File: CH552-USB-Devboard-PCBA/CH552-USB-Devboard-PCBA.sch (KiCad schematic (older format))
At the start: 42 parts, among them J1 Conn_01x11_Male, J2 Conn_01x11_Male, J3 USB_C_Receptacle, J4 USB_C_Receptacle, SW1 SW_Push, SW2 SW_Push, U2 CH552G, U3 TPS7A4101DGNT

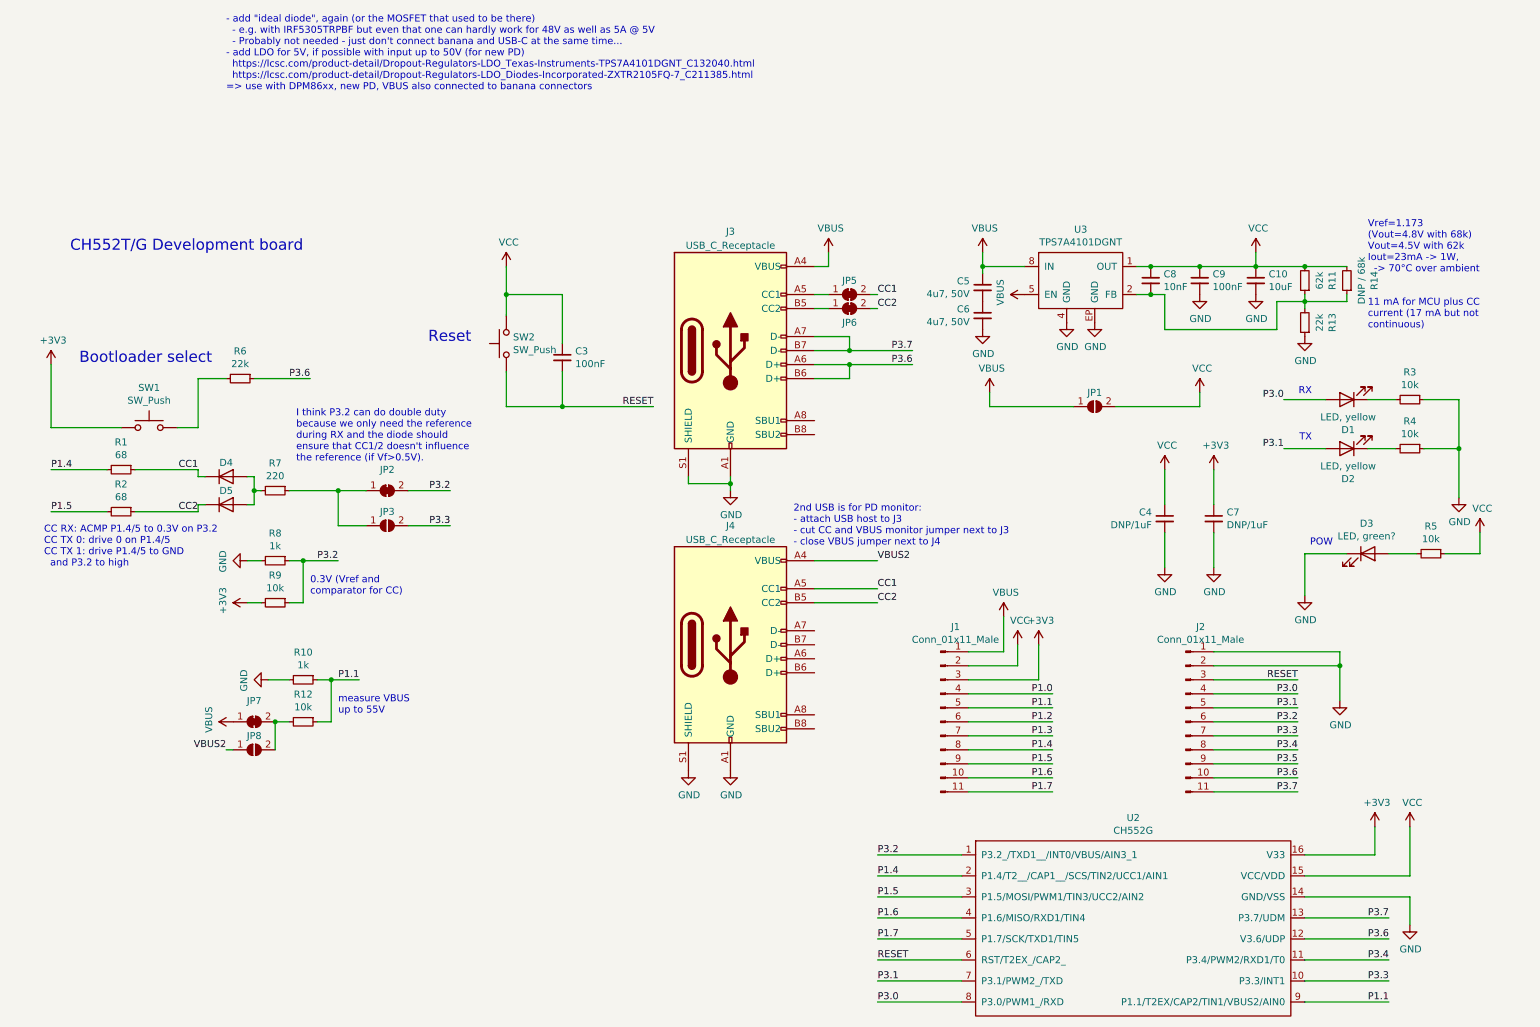
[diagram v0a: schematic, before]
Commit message: create variant for PCBA
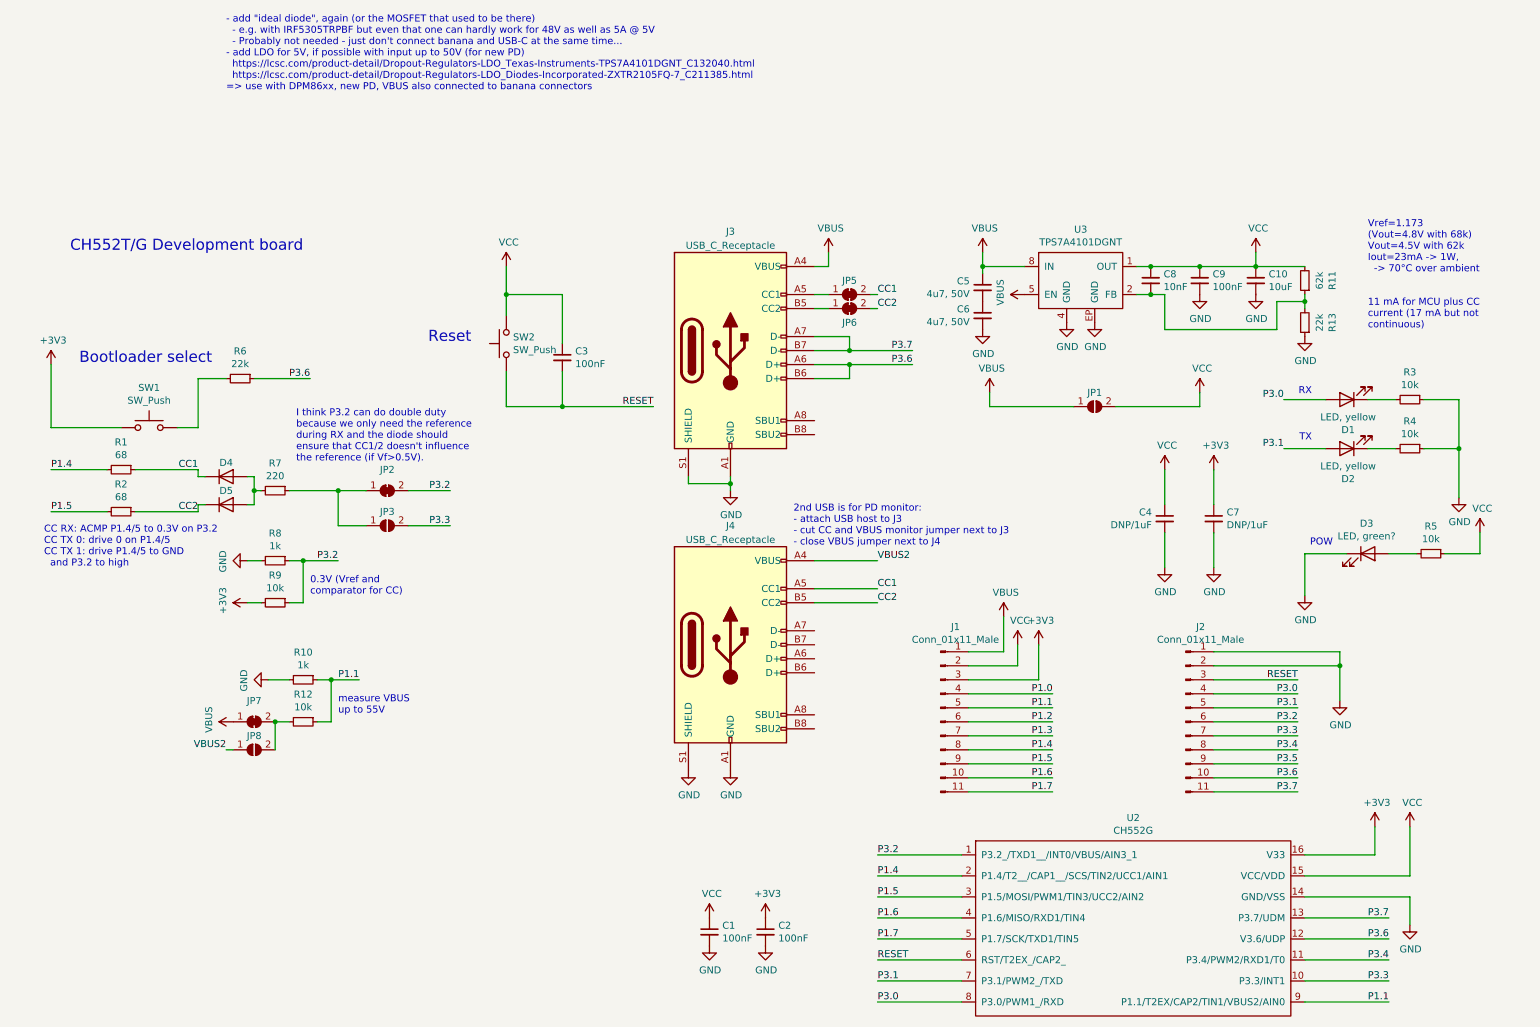
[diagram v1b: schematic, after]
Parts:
- removed R14: DNP / 68k, Resistor_SMD:R_0603_1608Metric_Pad1.05x0.95mm_HandSolder, symbol Device:R_Small
- added C1, C2: 100nF, Capacitor_SMD:C_0603_1608Metric_Pad1.05x0.95mm_HandSolder, symbol Device:C_Small
- J4: footprint footprint:VACON_CSP_USC16_TR -> CH552-USB-Devboard:Korean-Hroparts-Elec-TYPE-C-31-M-17; LCSC C165948 -> C283540
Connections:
- net +3V3: now also C2.1
- net GND: now also C1.2, C2.2
- net VCC: now also C1.1
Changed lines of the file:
@@
 EESchema Schematic File Version 4
+LIBS:CH552-USB-Devboard-PCBA-cache
 EELAYER 29 0
 EELAYER END
@@
 F 0 "J4" H 5650 4400 50  0000 C CNN
 F 1 "USB_C_Receptacle" H 5650 4300 50  0000 C CNN
-F 2 "footprint:VACON_CSP_USC16_TR" H 5800 3550 50  0001 C CNN
+F 2 "CH552-USB-Devboard:Korean-Hroparts-Elec-TYPE-C-31-M-17" H 5800 3550 50  0001 C CNN
 F 3 "http://www.usb.org/developers/docs/usb_31_033017.zip" H 5800 3550 50  0001 C CNN
-F 4 "C165948" H 5650 3550 50  0001 C CNN "LCSC"
+F 4 "C283540" H 5650 3550 50  0001 C CNN "LCSC"
 F 5 "PCBA" H 5650 3550 50  0001 C CNN "DNP"
 	1    5650 3550
@@
 Text Notes 10200 900  0    50   ~ 0
 Vref=1.173\n(Vout=4.8V with 68k)\nVout=4.5V with 62k\nIout=23mA -> 1W,\n  -> 70°C over ambient
-$Comp
-L Device:R_Small R14
-U 1 1 60E7CBB2
-P 10050 950
-F 0 "R14" V 9854 950 50  0000 C CNN
-F 1 "DNP / 68k" V 9945 950 50  0000 C CNN
-F 2 "Resistor_SMD:R_0603_1608Metric_Pad1.05x0.95mm_HandSolder" H 10050 950 50  0001 C CNN
-F 3 "~" H 10050 950 50  0001 C CNN
-F 4 "C23231" V 10050 950 50  0001 C CNN "LCSC"
-F 5 "1" V 10050 950 50  0001 C CNN "DNP"
-	1    10050 950
-	-1   0    0    1
-$EndComp
-Wire Wire Line
-	9750 1100 10050 1100
-Wire Wire Line
-	10050 1100 10050 1050
-Wire Wire Line
-	10050 850  9750 850
-Connection ~ 9750 850
 Text Notes 10200 1300 0    50   ~ 0
 11 mA for MCU plus CC\ncurrent (17 mA but not\ncontinuous)
@@
 	1    0    0    -1
 $EndComp
+$Comp
+L Device:C_Small C2
+U 1 1 60D50D65
+P 5900 5600
+F 0 "C2" H 5992 5646 50  0000 L CNN
+F 1 "100nF" H 5992 5555 50  0000 L CNN
+F 2 "Capacitor_SMD:C_0603_1608Metric_Pad1.05x0.95mm_HandSolder" H 5900 5600 50  0001 C CNN
+F 3 "~" H 5900 5600 50  0001 C CNN
+F 4 "C14663" H 5900 5600 50  0001 C CNN "LCSC"
+	1    5900 5600
+	1    0    0    -1
+$EndComp
+$Comp
+L power:GND #PWR?
+U 1 1 60D51335
+P 5900 5700
+F 0 "#PWR?" H 5900 5450 50  0001 C CNN
+F 1 "GND" H 5905 5527 50  0000 C CNN
+F 2 "" H 5900 5700 50  0001 C CNN
+F 3 "" H 5900 5700 50  0001 C CNN
+	1    5900 5700
+	1    0    0    -1
+$EndComp
+$Comp
+L power:+3V3 #PWR?
+U 1 1 60D515E1
+P 5900 5500
+F 0 "#PWR?" H 5900 5350 50  0001 C CNN
+F 1 "+3V3" H 5915 5673 50  0000 C CNN
+F 2 "" H 5900 5500 50  0001 C CNN
+F 3 "" H 5900 5500 50  0001 C CNN
+	1    5900 5500
+	1    0    0    -1
+$EndComp
+$Comp
+L Device:C_Small C1
+U 1 1 60D51BC0
+P 5500 5600
+F 0 "C1" H 5592 5646 50  0000 L CNN
+F 1 "100nF" H 5592 5555 50  0000 L CNN
+F 2 "Capacitor_SMD:C_0603_1608Metric_Pad1.05x0.95mm_HandSolder" H 5500 5600 50  0001 C CNN
+F 3 "~" H 5500 5600 50  0001 C CNN
+F 4 "C14663" H 5500 5600 50  0001 C CNN "LCSC"
+	1    5500 5600
+	1    0    0    -1
+$EndComp
+$Comp
+L power:GND #PWR?
+U 1 1 60D51BCA
+P 5500 5700
+F 0 "#PWR?" H 5500 5450 50  0001 C CNN
+F 1 "GND" H 5505 5527 50  0000 C CNN
+F 2 "" H 5500 5700 50  0001 C CNN
+F 3 "" H 5500 5700 50  0001 C CNN
+	1    5500 5700
+	1    0    0    -1
+$EndComp
+$Comp
+L power:VCC #PWR?
+U 1 1 60D5A817
+P 5500 5500
+F 0 "#PWR?" H 5500 5350 50  0001 C CNN
+F 1 "VCC" H 5517 5673 50  0000 C CNN
+F 2 "" H 5500 5500 50  0001 C CNN
+F 3 "" H 5500 5500 50  0001 C CNN
+	1    5500 5500
+	1    0    0    -1
+$EndComp

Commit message: replace LDO
I'm quite sure it wasn't out of stock three days ago...
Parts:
- added U1: ZXTR2105FQ, Package_TO_SOT_SMD:SOT-23, symbol CH552-USB-Devboard:ZXTR2105FQ
- C8, R11, R13, U3: DNP (none) -> 1
- J3, J4: symbol Connector:USB_C_Receptacle_USB2.0 -> CH552-USB-Devboard-PCBA-rescue:USB_C_Receptacle_USB2.0-Connector
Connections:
- net GND: now also U1.1 (GND)
- net VBUS: now also U1.3 (IN)
- net VCC: now also U1.2 (OUT)
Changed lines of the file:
@@
 EESchema Schematic File Version 4
-LIBS:CH552-USB-Devboard-PCBA-cache
-EELAYER 29 0
+EELAYER 30 0
 EELAYER END
 $Descr A4 11693 8268
@@
 	5650 2350 5650 2400
 $Comp
-L Connector:USB_C_Receptacle_USB2.0 J3
+L CH552-USB-Devboard-PCBA-rescue:USB_C_Receptacle_USB2.0-Connector J3
 U 1 1 5F0EEE62
 P 5650 1450
@@
 	2700 4100 2800 4100
 $Comp
-L Connector:USB_C_Receptacle_USB2.0 J4
+L CH552-USB-Devboard-PCBA-rescue:USB_C_Receptacle_USB2.0-Connector J4
 U 1 1 60C8CB0D
 P 5650 3550
@@
 F 3 "~" H 8650 950 50  0001 C CNN
 F 4 "C57112" H 8650 950 50  0001 C CNN "LCSC"
+F 5 "1" H 8650 950 50  0001 C CNN "DNP"
 	1    8650 950
 	1    0    0    -1
@@
 F 3 "~" H 9750 950 50  0001 C CNN
 F 4 "C23221" V 9750 950 50  0001 C CNN "LCSC"
+F 5 "1" V 9750 950 50  0001 C CNN "DNP"
 	1    9750 950
 	-1   0    0    1
@@
 F 3 "~" H 9750 1250 50  0001 C CNN
 F 4 "C31850" V 9750 1250 50  0001 C CNN "LCSC"
+F 5 "1" V 9750 1250 50  0001 C CNN "DNP"
 	1    9750 1250
 	-1   0    0    1
@@
 F 3 "https://www.ti.com/lit/ds/symlink/tps7a4101.pdf?ts=1623464240651&ref_url=https%253A%252F%252Fwww.ti.com%252F" H 8150 950 50  0001 C CNN
 F 4 "C132040" H 8150 950 50  0001 C CNN "LCSC"
+F 5 "1" H 8150 950 50  0001 C CNN "DNP"
 	1    8150 950
 	1    0    0    -1
@@
 $EndComp
 $Comp
-L power:GND #PWR?
+L power:GND #PWR0105
 U 1 1 60D51335
 P 5900 5700
-F 0 "#PWR?" H 5900 5450 50  0001 C CNN
+F 0 "#PWR0105" H 5900 5450 50  0001 C CNN
 F 1 "GND" H 5905 5527 50  0000 C CNN
 F 2 "" H 5900 5700 50  0001 C CNN
@@
 $EndComp
 $Comp
-L power:+3V3 #PWR?
+L power:+3V3 #PWR0106
 U 1 1 60D515E1
 P 5900 5500
-F 0 "#PWR?" H 5900 5350 50  0001 C CNN
+F 0 "#PWR0106" H 5900 5350 50  0001 C CNN
 F 1 "+3V3" H 5915 5673 50  0000 C CNN
 F 2 "" H 5900 5500 50  0001 C CNN
@@
 $EndComp
 $Comp
-L power:GND #PWR?
+L power:GND #PWR0107
 U 1 1 60D51BCA
 P 5500 5700
-F 0 "#PWR?" H 5500 5450 50  0001 C CNN
+F 0 "#PWR0107" H 5500 5450 50  0001 C CNN
 F 1 "GND" H 5505 5527 50  0000 C CNN
 F 2 "" H 5500 5700 50  0001 C CNN
@@
 $EndComp
 $Comp
-L power:VCC #PWR?
+L power:VCC #PWR0108
 U 1 1 60D5A817
 P 5500 5500
-F 0 "#PWR?" H 5500 5350 50  0001 C CNN
+F 0 "#PWR0108" H 5500 5350 50  0001 C CNN
 F 1 "VCC" H 5517 5673 50  0000 C CNN
 F 2 "" H 5500 5500 50  0001 C CNN
@@
 	1    0    0    -1
 $EndComp
+$Comp
+L CH552-USB-Devboard:ZXTR2105FQ U1
+U 1 1 60CC6478
+P 7850 2150
+F 0 "U1" H 7850 2392 50  0000 C CNN
+F 1 "ZXTR2105FQ" H 7850 2301 50  0000 C CNN
+F 2 "Package_TO_SOT_SMD:SOT-23" H 7875 2000 50  0001 L CIN
+F 3 "https://datasheet.lcsc.com/lcsc/1809081633_Diodes-Incorporated-ZXTR2105FQ-7_C211385.pdf" H 7850 2100 50  0001 C CNN
+F 4 "C211385" H 7850 2150 50  0001 C CNN "LCSC"
+	1    7850 2150
+	1    0    0    -1
+$EndComp
+$Comp
+L power:GND #PWR0109
+U 1 1 60CD546D
+P 7850 2450
+F 0 "#PWR0109" H 7850 2200 50  0001 C CNN
+F 1 "GND" H 7855 2277 50  0000 C CNN
+F 2 "" H 7850 2450 50  0001 C CNN
+F 3 "" H 7850 2450 50  0001 C CNN
+	1    7850 2450
+	1    0    0    -1
+$EndComp
+$Comp
+L power:VBUS #PWR0141
+U 1 1 60CD5D53
+P 7550 2150
+F 0 "#PWR0141" H 7550 2000 50  0001 C CNN
+F 1 "VBUS" H 7565 2323 50  0000 C CNN
+F 2 "" H 7550 2150 50  0001 C CNN
+F 3 "" H 7550 2150 50  0001 C CNN
+	1    7550 2150
+	0    -1   -1   0
+$EndComp
+$Comp
+L power:VCC #PWR0142
+U 1 1 60CD684D
+P 8150 2150
+F 0 "#PWR0142" H 8150 2000 50  0001 C CNN
+F 1 "VCC" H 8167 2323 50  0000 C CNN
+F 2 "" H 8150 2150 50  0001 C CNN
+F 3 "" H 8150 2150 50  0001 C CNN
+	1    8150 2150
+	0    1    1    0
+$EndComp
 $EndSCHEMATC
